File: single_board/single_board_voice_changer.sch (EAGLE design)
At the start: 20 parts, among them U1 ATMEGA328P_PDIP

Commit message: save
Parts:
- added C6: 0.1uF, SparkFun-Capacitors:CAPPTH
- added INPUT1, INPUT2, INPUT3, INPUT4: (no value), SparkFun-Connectors:M03PTH
- added R6: 10K, SparkFun-Passives:RESISTORPTH-1/4W
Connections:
- net ADC_CH0: now also INPUT1.2
- net ADC_CH1: now also INPUT2.2
- net ADC_CH2: now also INPUT3.2
- net ADC_CH3: now also INPUT4.2
- net DTR: now also C6.1
- net GND: now also INPUT1.1, INPUT2.1, INPUT3.1, INPUT4.1
- net RESET: now also C6.2, R6.1, U1.PC6(/RESET)
- net RX: now also U1.PD0(RXD)
- net TX: now also U1.PD1(TXD)
- net VCC: now also R6.2
- net VREF: now also INPUT1.3, INPUT2.3, INPUT3.3, INPUT4.3
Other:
- moved on the sheet: C3, IC1, JP1, U$3

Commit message: working on single board version
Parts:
- U$3: value V_REG_LD1117VXX -> MCP1702-3302E/TO; device SparkFun-PowerIC:V_REG_LD1117VXX -> Microchip_By_element14_Batch_1:MCP1702-3302E/TO
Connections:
- net VCC: now also U$3.VIN; no longer U$3.IN
- net VREF: now also U$3.VOUT; no longer U$3.OUT
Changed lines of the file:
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@@
 <part name="GND10" library="SparkFun-Aesthetics" deviceset="GND" device=""/>
 <part name="SUPPLY1" library="SparkFun-Aesthetics" deviceset="VCC" device=""/>
-<part name="U$3" library="SparkFun-PowerIC" deviceset="V_REG_LD1117VXX" device=""/>
 <part name="SUPPLY2" library="SparkFun-Aesthetics" deviceset="VCC" device=""/>
 <part name="GND11" library="SparkFun-Aesthetics" deviceset="GND" device=""/>
@@
 <part name="INPUT3" library="SparkFun-Connectors" deviceset="M03" device="PTH"/>
 <part name="INPUT4" library="SparkFun-Connectors" deviceset="M03" device="PTH"/>
+<part name="U$3" library="Microchip_By_element14_Batch_1" deviceset="MCP1702-3302E/TO" device=""/>
 </parts>
 <sheets>
@@
 <instance part="GND10" gate="1" x="-27.94" y="91.44"/>
 <instance part="SUPPLY1" gate="G$1" x="-17.78" y="106.68"/>
-<instance part="U$3" gate="G$1" x="-5.08" y="104.14"/>
 <instance part="SUPPLY2" gate="G$1" x="25.4" y="63.5"/>
-<instance part="GND11" gate="1" x="-5.08" y="91.44"/>
+<instance part="GND11" gate="1" x="-7.62" y="91.44"/>
 <instance part="GND12" gate="1" x="-17.78" y="88.9"/>
 <instance part="C3" gate="G$1" x="-17.78" y="96.52"/>
@@
 <instance part="INPUT3" gate="G$1" x="48.26" y="-30.48"/>
 <instance part="INPUT4" gate="G$1" x="73.66" y="-30.48"/>
+<instance part="U$3" gate="A" x="12.7" y="104.14"/>
 </instances>
 <busses>
@@
 </segment>
 <segment>
-<pinref part="GND11" gate="1" pin="GND"/>
-<pinref part="U$3" gate="G$1" pin="GND"/>
-<wire x1="-5.08" y1="93.98" x2="-5.08" y2="96.52" width="0.1524" layer="91"/>
-</segment>
-<segment>
 <pinref part="GND12" gate="1" pin="GND"/>
 <pinref part="C3" gate="G$1" pin="2"/>
@@
 <wire x1="81.28" y1="-33.02" x2="91.44" y2="-33.02" width="0.1524" layer="91"/>
 <label x="81.28" y="-33.02" size="1.778" layer="95"/>
+</segment>
+<segment>
+<pinref part="U$3" gate="A" pin="GND"/>
+<wire x1="-5.08" y1="99.06" x2="-7.62" y2="99.06" width="0.1524" layer="91"/>
+<pinref part="GND11" gate="1" pin="GND"/>
+<wire x1="-7.62" y1="99.06" x2="-7.62" y2="93.98" width="0.1524" layer="91"/>
 </segment>
 </net>
@@
 <wire x1="-17.78" y1="104.14" x2="-17.78" y2="106.68" width="0.1524" layer="91"/>
 <junction x="-17.78" y="104.14"/>
-<pinref part="U$3" gate="G$1" pin="IN"/>
-<wire x1="-17.78" y1="104.14" x2="-12.7" y2="104.14" width="0.1524" layer="91"/>
 <pinref part="C3" gate="G$1" pin="1"/>
 <wire x1="-17.78" y1="101.6" x2="-17.78" y2="104.14" width="0.1524" layer="91"/>
+<pinref part="U$3" gate="A" pin="VIN"/>
+<wire x1="-5.08" y1="104.14" x2="-17.78" y2="104.14" width="0.1524" layer="91"/>
 </segment>
 <segment>
@@
 </segment>
 <segment>
-<pinref part="U$3" gate="G$1" pin="OUT"/>
-<wire x1="2.54" y1="104.14" x2="12.7" y2="104.14" width="0.1524" layer="91"/>
-<label x="2.54" y="104.14" size="1.778" layer="95"/>
-</segment>
-<segment>
 <pinref part="INPUT1" gate="G$1" pin="3"/>
 <wire x1="5.08" y1="-27.94" x2="15.24" y2="-27.94" width="0.1524" layer="91"/>
@@
 <label x="81.28" y="-27.94" size="1.778" layer="95"/>
 </segment>
-</net>
+<segment>
+<pinref part="U$3" gate="A" pin="VOUT"/>
+<wire x1="30.48" y1="101.6" x2="45.72" y2="101.6" width="0.1524" layer="91"/>
+<label x="33.02" y="101.6" size="1.778" layer="95"/>
+</segment>
+</net>

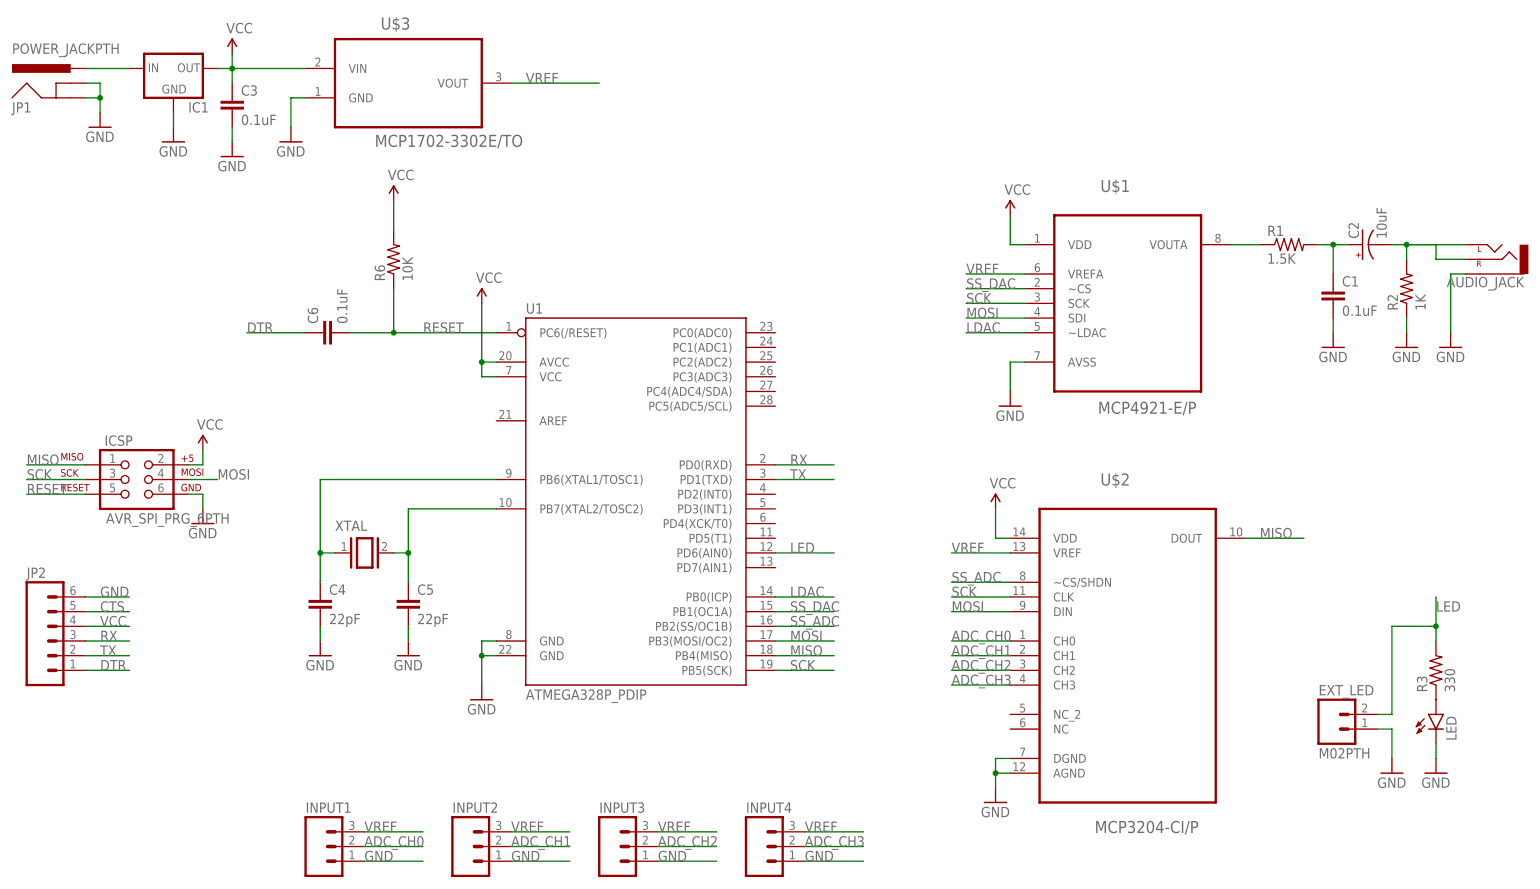
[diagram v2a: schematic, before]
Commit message: change ADC to MCP3202
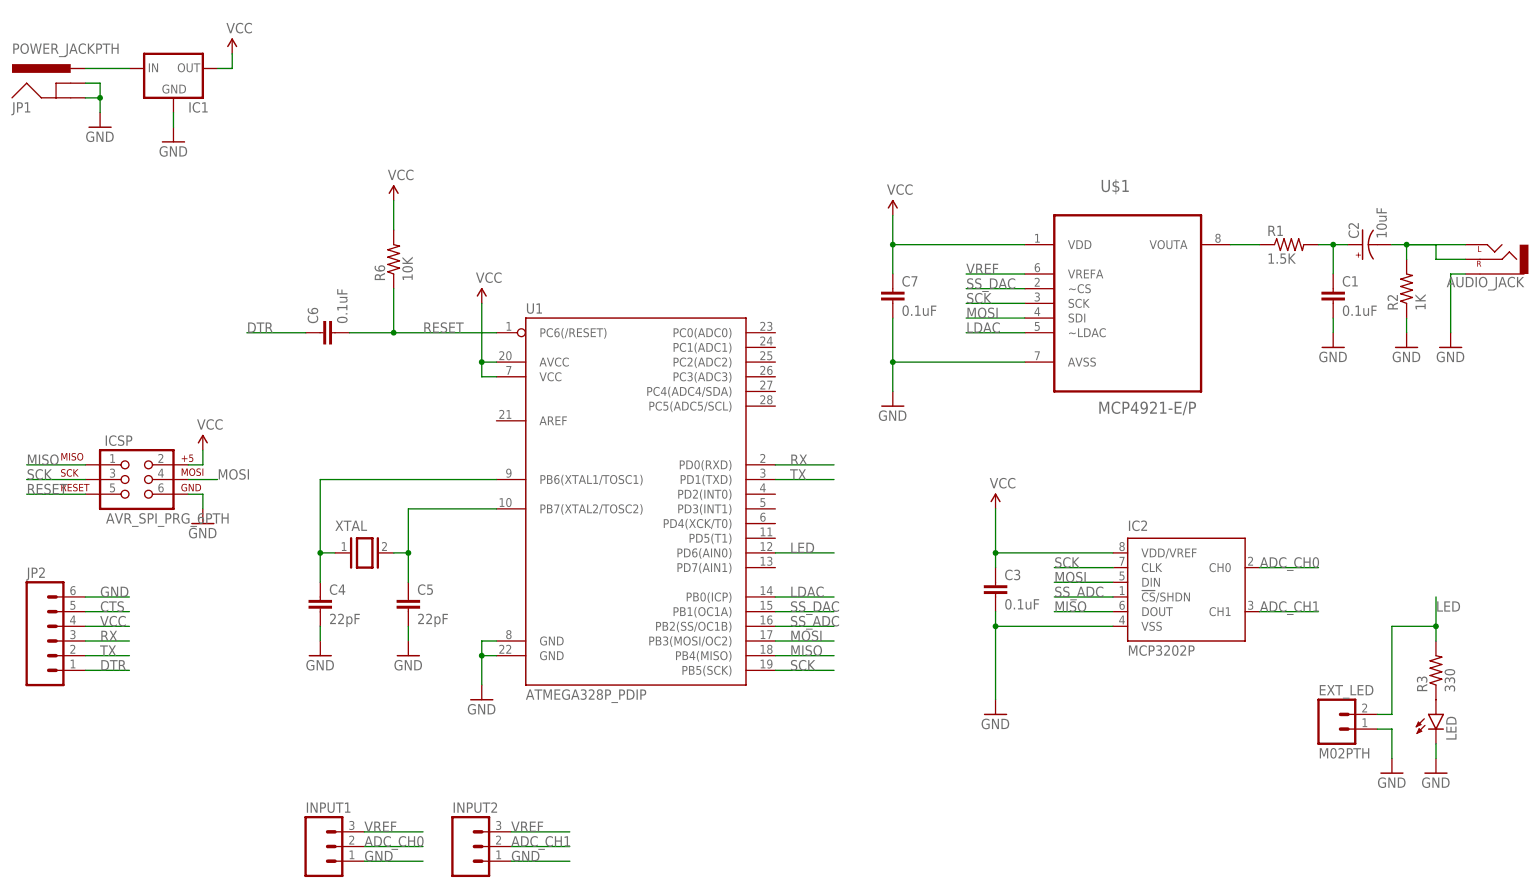
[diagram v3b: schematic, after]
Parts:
- removed INPUT3, INPUT4: (no value), SparkFun-Connectors:M03PTH
- removed U$2: MCP3204-CI/P, Microchip_By_element14_Batch_1:MCP3204-CI/P
- removed U$3: MCP1702-3302E/TO, Microchip_By_element14_Batch_1:MCP1702-3302E/TO
- added C7: 0.1uF, SparkFun-Passives:CAPPTH
- added IC2: MCP3202P, microchip:MCP3202P
- C3: device SparkFun-Capacitors:CAPPTH -> SparkFun-Passives:CAPPTH
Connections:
- removed net ADC_CH2: INPUT3.2, U$2.CH2
- removed net ADC_CH3: INPUT4.2, U$2.CH3
- net ADC_CH0: now also IC2.CH0; no longer U$2.CH0
- net ADC_CH1: now also IC2.CH1; no longer U$2.CH1
- net GND: now also C7.2, IC2.VSS; no longer INPUT3.1, INPUT4.1, U$2.AGND, U$2.DGND, U$3.GND
- net MISO: now also IC2.DOUT; no longer U$2.DOUT
- net MOSI: now also IC2.DIN; no longer U$2.DIN
- net SCK: now also IC2.CLK; no longer U$2.CLK
- net SS_ADC: now also IC2.!CS!/SHDN; no longer U$2.~CS/SHDN
- net VCC: now also C7.1, IC2.VDD/VREF; no longer U$2.VDD, U$3.VIN
- net VREF: no longer INPUT3.3, INPUT4.3, U$2.VREF, U$3.VOUT
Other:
- moved on the sheet: C3

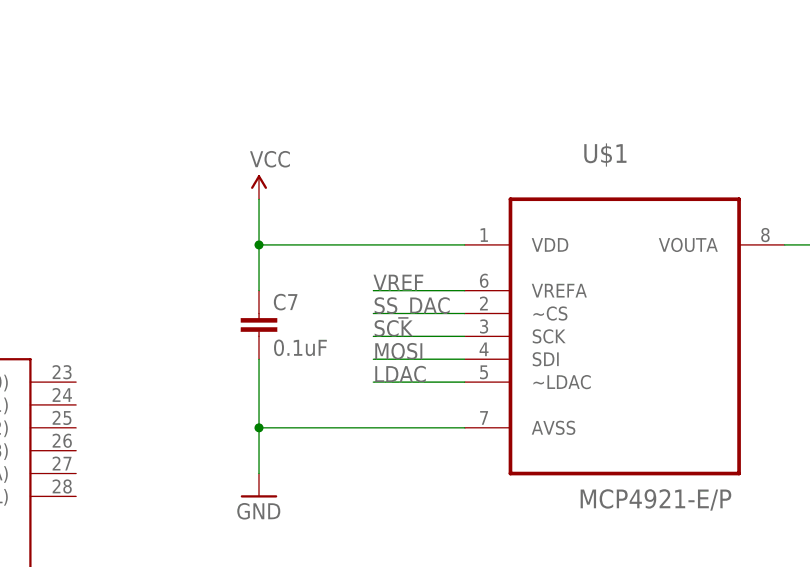
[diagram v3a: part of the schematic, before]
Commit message: consistent fonts
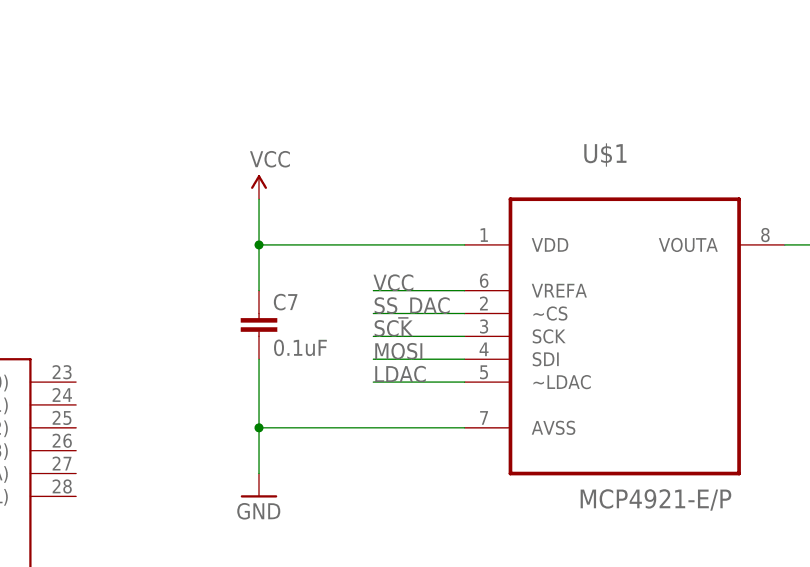
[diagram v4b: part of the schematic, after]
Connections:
- net VCC: now also U$1.VREFA
- net VREF: no longer U$1.VREFA
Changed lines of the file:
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@@
 <wire x1="96.52" y1="73.66" x2="96.52" y2="68.58" width="0.1524" layer="91"/>
+</segment>
+<segment>
+<pinref part="U$1" gate="A" pin="VREFA"/>
+<wire x1="119.38" y1="68.58" x2="109.22" y2="68.58" width="0.1524" layer="91"/>
+<label x="109.22" y="68.58" size="1.778" layer="95"/>
 </segment>
 </net>
@@
 <net name="VREF" class="0">
 <segment>
-<pinref part="U$1" gate="A" pin="VREFA"/>
-<wire x1="119.38" y1="68.58" x2="109.22" y2="68.58" width="0.1524" layer="91"/>
-<label x="109.22" y="68.58" size="1.778" layer="95"/>
-</segment>
-<segment>
 <pinref part="INPUT1" gate="G$1" pin="3"/>

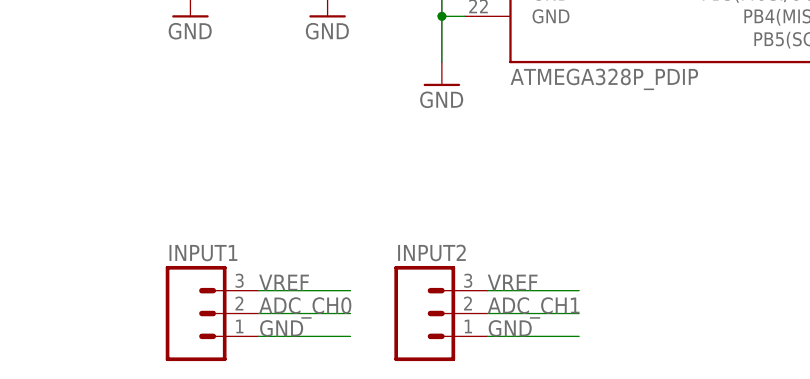
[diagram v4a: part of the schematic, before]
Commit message: fix error with schematic
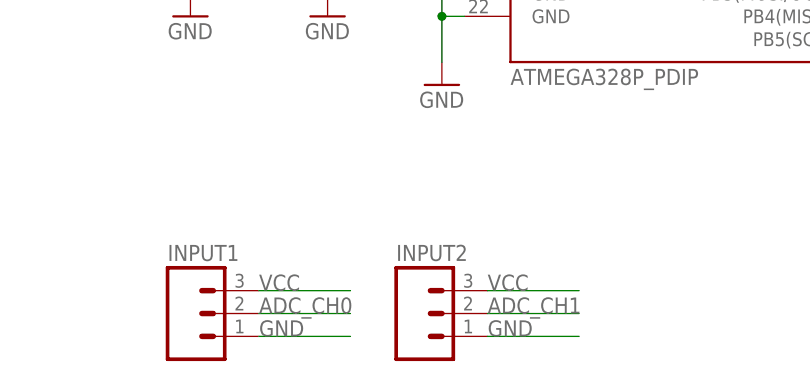
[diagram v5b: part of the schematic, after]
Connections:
- removed net VREF: INPUT1.3, INPUT2.3
- net VCC: now also INPUT1.3, INPUT2.3
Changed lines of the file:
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@@
 <label x="109.22" y="68.58" size="1.778" layer="95"/>
+</segment>
+<segment>
+<pinref part="INPUT1" gate="G$1" pin="3"/>
+<wire x1="5.08" y1="-27.94" x2="15.24" y2="-27.94" width="0.1524" layer="91"/>
+<label x="5.08" y="-27.94" size="1.778" layer="95"/>
+</segment>
+<segment>
+<pinref part="INPUT2" gate="G$1" pin="3"/>
+<wire x1="30.48" y1="-27.94" x2="40.64" y2="-27.94" width="0.1524" layer="91"/>
+<label x="30.48" y="-27.94" size="1.778" layer="95"/>
 </segment>
 </net>
@@
 </segment>
 </net>
-<net name="VREF" class="0">
-<segment>
-<pinref part="INPUT1" gate="G$1" pin="3"/>
-<wire x1="5.08" y1="-27.94" x2="15.24" y2="-27.94" width="0.1524" layer="91"/>
-<label x="5.08" y="-27.94" size="1.778" layer="95"/>
-</segment>
-<segment>
-<pinref part="INPUT2" gate="G$1" pin="3"/>
-<wire x1="30.48" y1="-27.94" x2="40.64" y2="-27.94" width="0.1524" layer="91"/>
-<label x="30.48" y="-27.94" size="1.778" layer="95"/>
-</segment>
-</net>
